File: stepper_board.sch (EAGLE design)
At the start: 60 parts, among them IC1 MCP1703DB, Y1 12 MHz

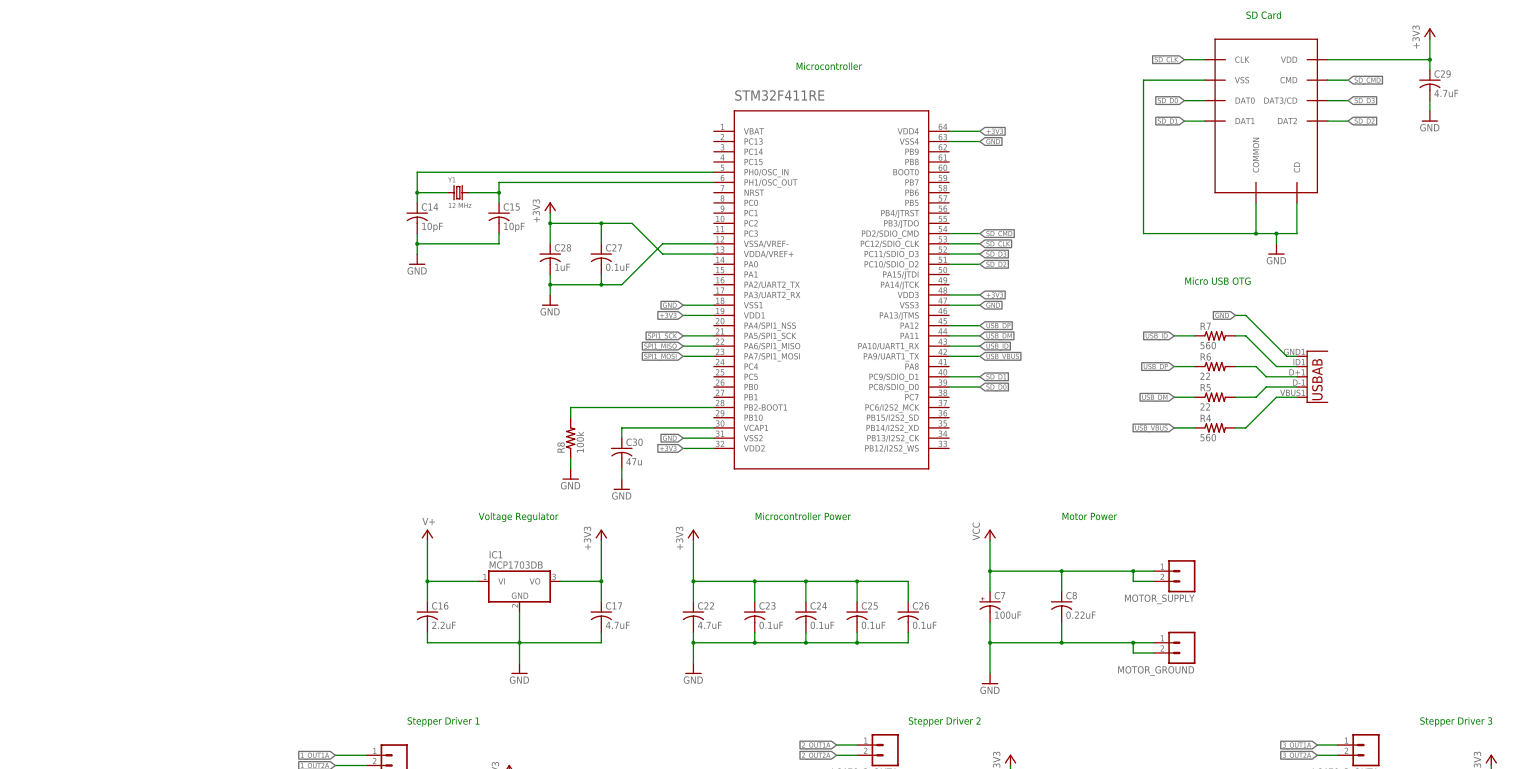
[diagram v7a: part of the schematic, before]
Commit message: Added ESD Protection and STM documentation
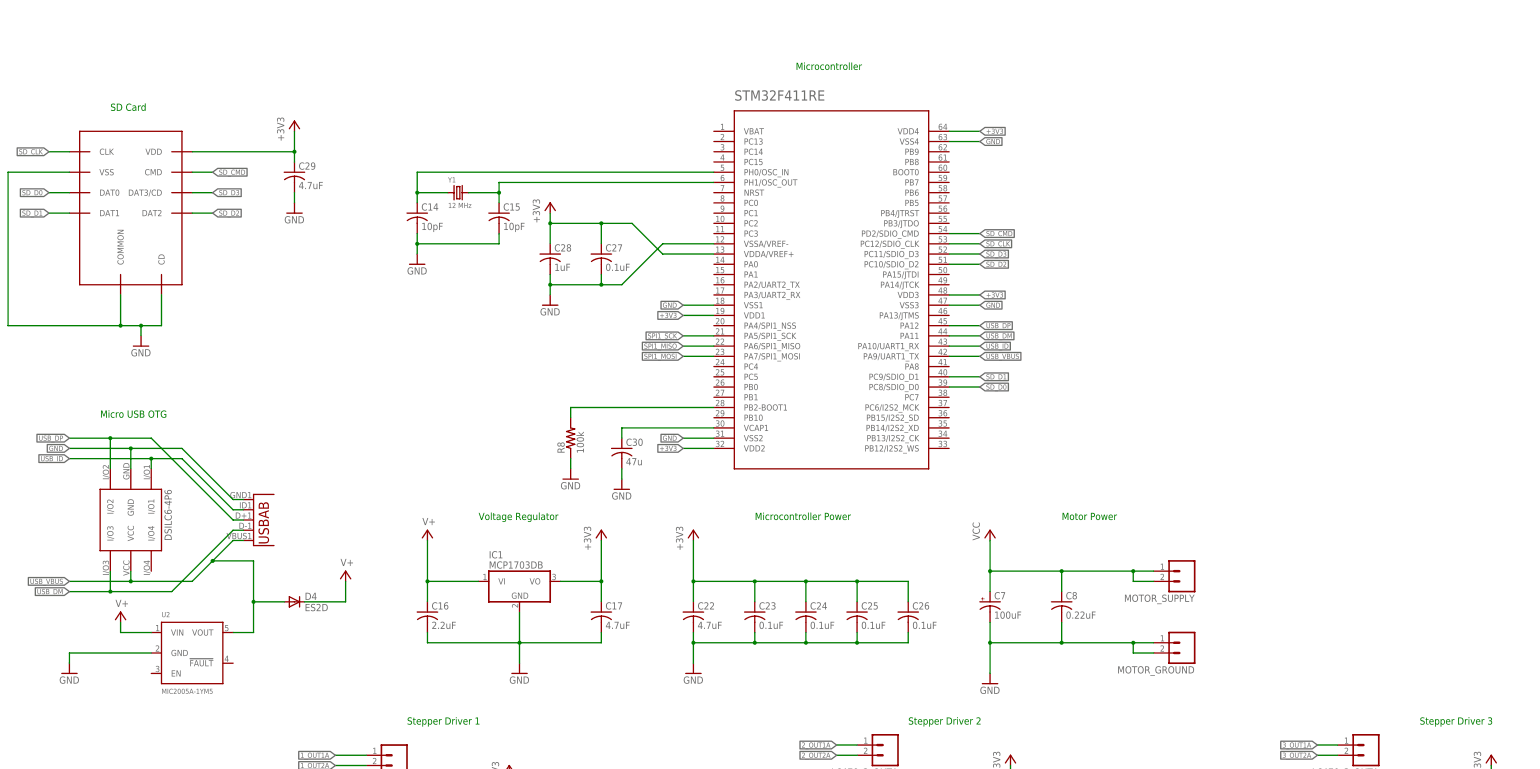
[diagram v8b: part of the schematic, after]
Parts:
- removed R4, R7: 560, rcl:R-US_R0805
- removed R5, R6: 22, rcl:R-US_R0805
- added D4: ES2D, diode:ES2D
- added U$1: DSILC6-4P6, Stepper_Driver:DSILC6-4P6
- added U2: MIC2005A-1YM5, Power_Switch:MIC2005A-1YM5
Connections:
- removed net N$18: R4.2, U1.VBUS
- removed net N$19: R5.2, U1.D-
- removed net N$20: R6.2, U1.D+
- removed net N$21: R7.2, U1.USBID
- net GND: now also U$1.GND, U2.GND
- net USB_DM: now also U$1.I/O3, U1.D-; no longer R5.1
- net USB_DP: now also U$1.I/O2, U1.D+; no longer R6.1
- net USB_ID: now also U$1.I/O1, U1.USBID; no longer R7.1
- net USB_VBUS: now also D4.A, U$1.VCC, U1.VBUS, U2.VOUT; no longer R4.1
- net V+: now also D4.C, U2.VIN
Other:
- moved on the sheet: C29
